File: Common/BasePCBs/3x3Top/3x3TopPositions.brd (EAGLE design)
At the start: 100 x 80 mm, 11 parts, among them CON1 SHIELD_FINGER0820, CON2 SHIELD_FINGER0820, CON3 SHIELD_FINGER0820, CON4 SHIELD_FINGER0820, CON5 SHIELD_FINGER0820, CON6 SHIELD_FINGER0820, CON7 SHIELD_FINGER0820, CON8 SHIELD_FINGER0820, CON9 SHIELD_FINGER0820

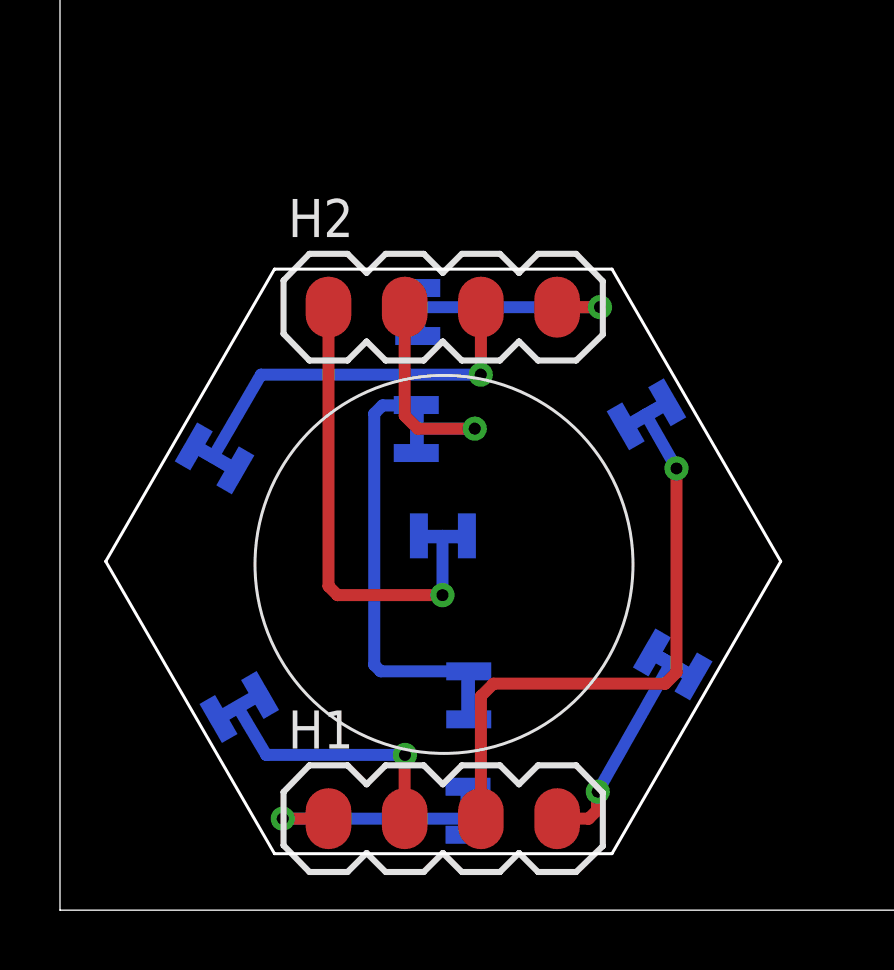
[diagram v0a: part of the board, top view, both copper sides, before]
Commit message: Added programmable module's top PCB
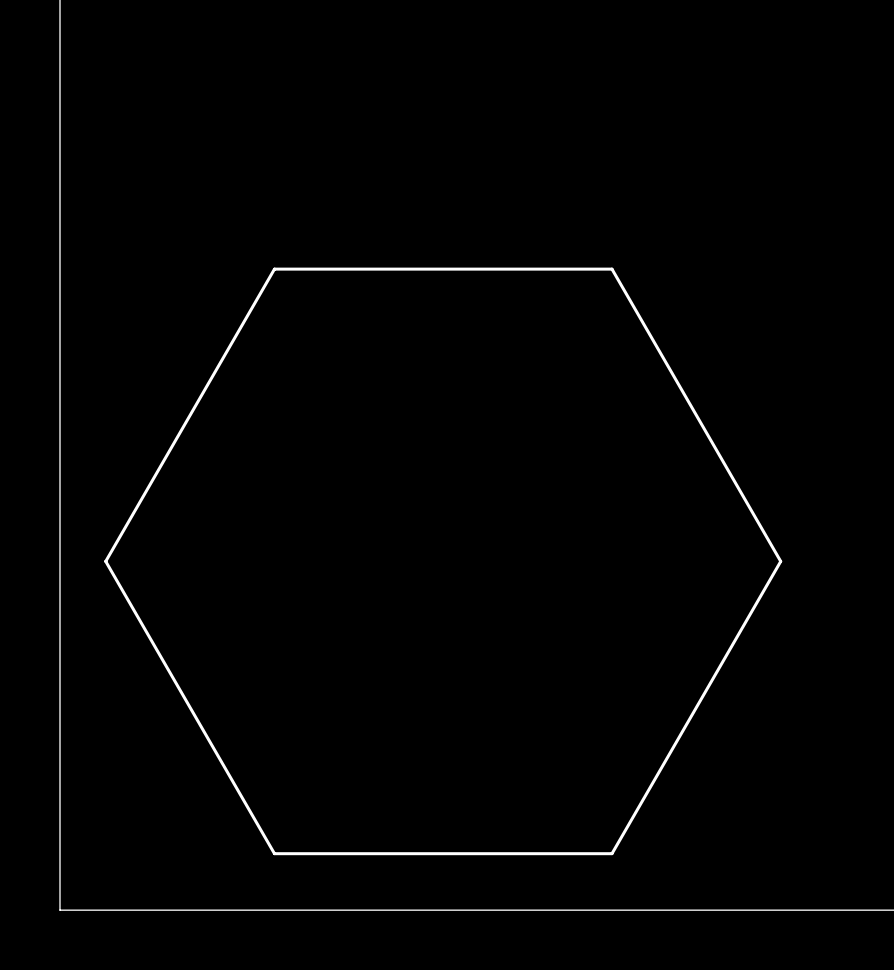
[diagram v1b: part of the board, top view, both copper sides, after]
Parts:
- removed CON1, CON2, CON3, CON4, CON5, CON6, CON7, CON8, CON9: SHIELD_FINGER0820, MakerShoe:SHIELD_FINGER_PKG
- removed H1, H2: (no value), SparkFun-Connectors:1X04_NO_HOLES
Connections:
- removed net GND: CON3.P1, CON3.P2, H2.1
- removed net PWR: CON1.P1, CON1.P2, CON2.P1, CON2.P2, H2.2
- removed net SIN1: CON7.P1, CON7.P2, H1.4
- removed net SIN2: CON8.P1, CON8.P2, H1.2
- removed net SIN3: CON9.P1, CON9.P2, H2.4
- removed net SOUT1: CON4.P1, CON4.P2, H1.3
- removed net SOUT2: CON5.P1, CON5.P2, H1.1
- removed net SOUT3: CON6.P1, CON6.P2, H2.3
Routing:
- net PWR: track 25.2 -> 0.00 mm, vias 1 -> 0
- net SOUT1: track 21.4 -> 0.00 mm, vias 1 -> 0
- net GND: track 16.8 -> 0.00 mm, vias 1 -> 0
- net SOUT3: track 14.4 -> 0.00 mm, vias 1 -> 0
- net SIN2: track 10.2 -> 0.00 mm, vias 1 -> 0
- net SIN1: track 9.31 -> 0.00 mm, vias 1 -> 0
- net SOUT2: track 9.30 -> 0.00 mm, vias 1 -> 0
- net SIN3: track 9.11 -> 0.00 mm, vias 1 -> 0
